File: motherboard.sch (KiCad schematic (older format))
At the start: 1 part

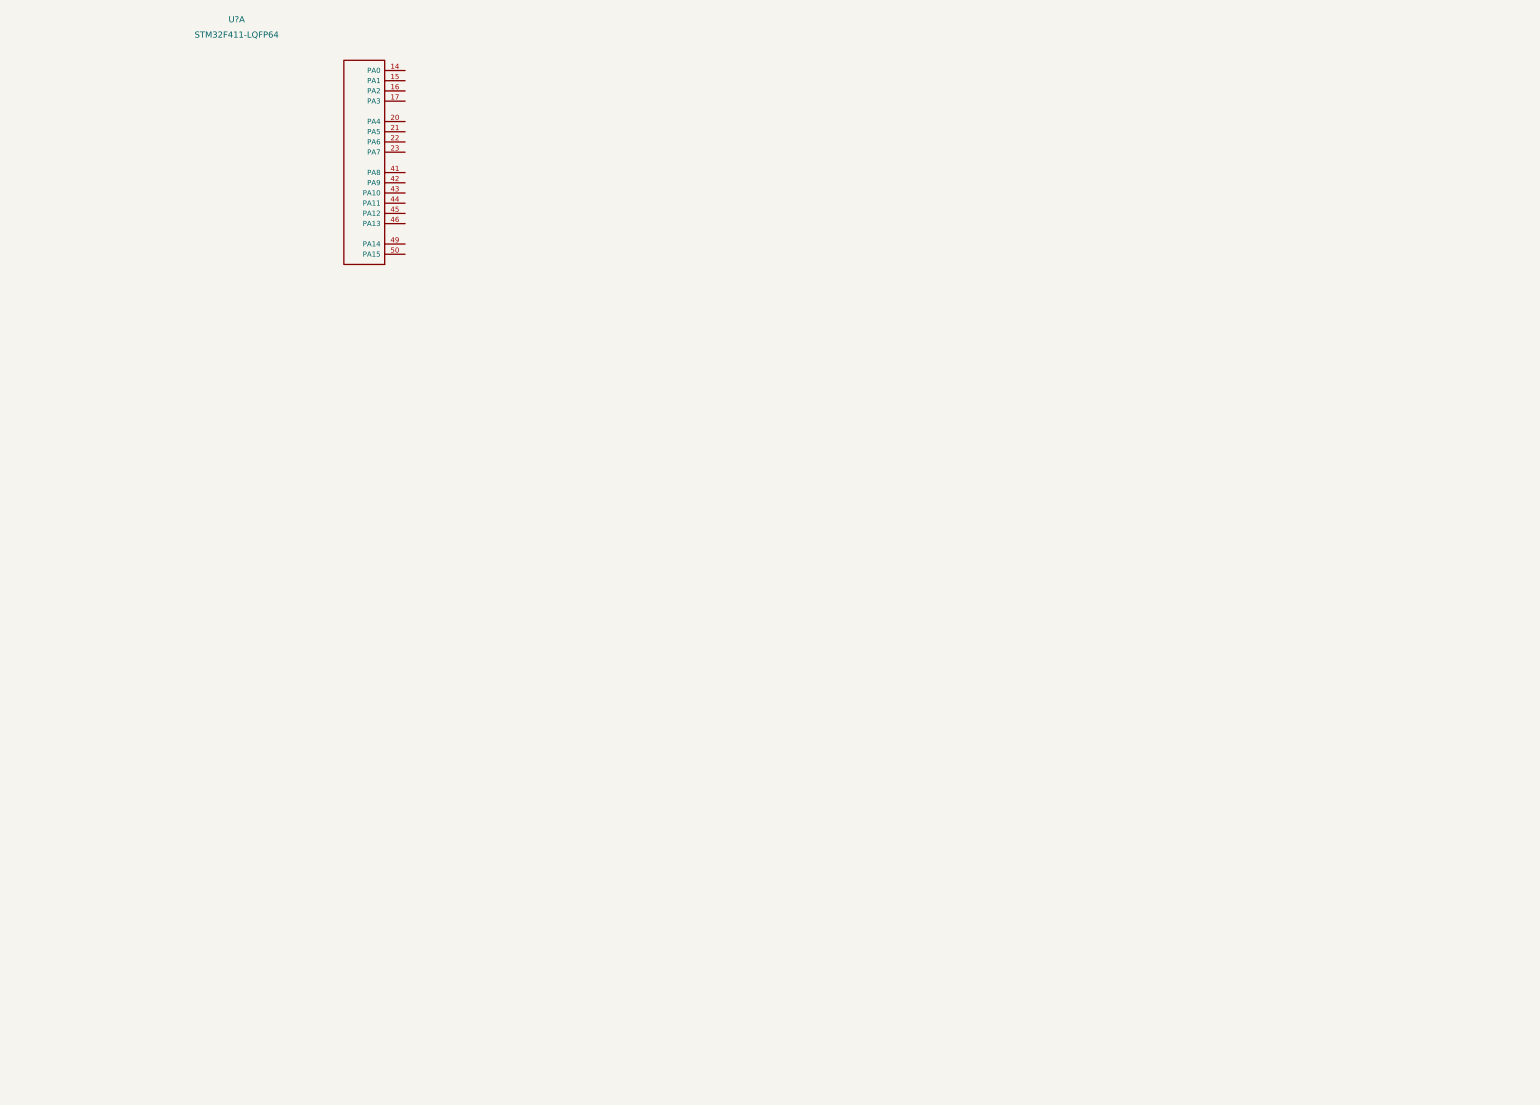
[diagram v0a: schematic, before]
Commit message: Work done on buffers and MCU placement
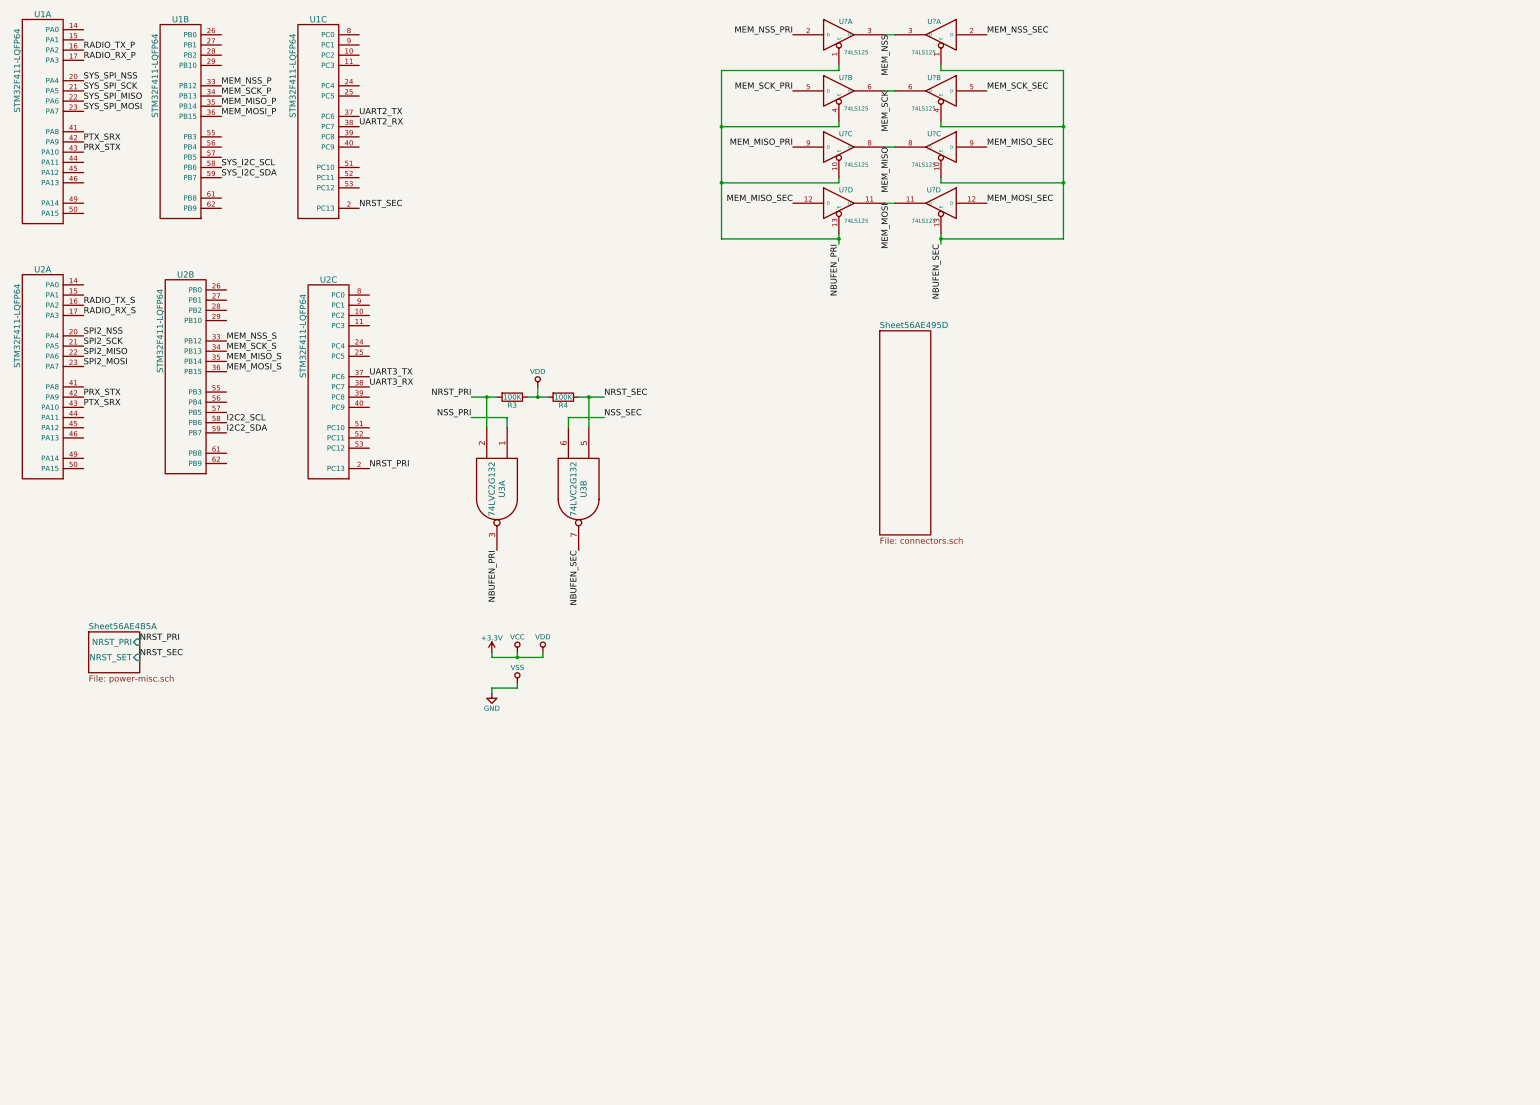
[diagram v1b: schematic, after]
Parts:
- removed U?: STM32F411-LQFP64, symbol STM32F411-LQFP64
- added R3, R4: 100K, symbol R
- added U1, U2: STM32F411-LQFP64, symbol STM32F411-LQFP64
- added U3: 74LVC2G132, symbol 74LVC2G132
- added U? (x8): 74LS125, symbol 74LS125
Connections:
- new net +3V3: R3.1, R4.2, U3.8 (VCC), U3.8 (VCC), U?.14 (VCC), U?.14 (VCC), U?.14 (VCC), U?.14 (VCC), U?.14 (VCC), U?.14 (VCC), U?.14 (VCC), U?.14 (VCC)
- new net GND: U3.4 (GND), U3.4 (GND), U?.7 (GND), U?.7 (GND), U?.7 (GND), U?.7 (GND), U?.7 (GND), U?.7 (GND), U?.7 (GND), U?.7 (GND)
- new net I2C2_SCL: U2.58 (PB6)
- new net I2C2_SDA: U2.59 (PB7)
- new net MEM_MISO: U?.8 (O), U?.8 (O)
- new net MEM_MISO_P: U1.35 (PB14)
- new net MEM_MISO_PRI: U?.9 (D)
- new net MEM_MISO_S: U2.35 (PB14)
- new net MEM_MISO_SEC: U?.12 (D), U?.9 (D)
- new net MEM_MOSI: U?.11 (O), U?.11 (O)
- new net MEM_MOSI_P: U1.36 (PB15)
- new net MEM_MOSI_S: U2.36 (PB15)
- new net MEM_MOSI_SEC: U?.12 (D)
- new net MEM_NSS: U?.3 (O), U?.3 (O)
- new net MEM_NSS_P: U1.33 (PB12)
- new net MEM_NSS_PRI: U?.2 (D)
- new net MEM_NSS_S: U2.33 (PB12)
- new net MEM_NSS_SEC: U?.2 (D)
- new net MEM_SCK: U?.6 (O), U?.6 (O)
- new net MEM_SCK_P: U1.34 (PB13)
- new net MEM_SCK_PRI: U?.5 (D)
- new net MEM_SCK_S: U2.34 (PB13)
- new net MEM_SCK_SEC: U?.5 (D)
- new net NBUFEN_PRI: U3.3, U?.1 (E), U?.10 (E), U?.13 (E), U?.4 (E)
- new net NBUFEN_SEC: U3.7, U?.1 (E), U?.10 (E), U?.13 (E), U?.4 (E)
- new net NRST_PRI: R3.2, U2.2 (PC13), U3.2
- new net NRST_SEC: R4.1, U1.2 (PC13), U3.5
- new net NSS_PRI: U3.1
- new net NSS_SEC: U3.6
- new net PRX_STX: U1.43 (PA10), U2.42 (PA9)
- new net PTX_SRX: U1.42 (PA9), U2.43 (PA10)
- new net RADIO_RX_P: U1.17 (PA3)
- new net RADIO_RX_S: U2.17 (PA3)
- new net RADIO_TX_P: U1.16 (PA2)
- new net RADIO_TX_S: U2.16 (PA2)
- new net SPI2_MISO: U2.22 (PA6)
- new net SPI2_MOSI: U2.23 (PA7)
- new net SPI2_NSS: U2.20 (PA4)
- new net SPI2_SCK: U2.21 (PA5)
- new net SYS_I2C_SCL: U1.58 (PB6)
- new net SYS_I2C_SDA: U1.59 (PB7)
- new net SYS_SPI_MISO: U1.22 (PA6)
- new net SYS_SPI_MOSI: U1.23 (PA7)
- new net SYS_SPI_NSS: U1.20 (PA4)
- new net SYS_SPI_SCK: U1.21 (PA5)
- new net UART2_RX: U1.38 (PC7)
- new net UART2_TX: U1.37 (PC6)
- new net UART3_RX: U2.38 (PC7)
- new net UART3_TX: U2.37 (PC6)

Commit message: Did some stuff
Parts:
- added R? (x2): 100K, symbol R
- added U? (x4): 74LS125, symbol 74LS125
- gave numbers to parts that had none: 2
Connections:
- net +3V3: now also U4.13 (E), U5.13 (E), R?.2, R?.2, U?.14 (VCC), U?.14 (VCC), U?.14 (VCC), U?.14 (VCC)
- net GND: now also U?.7 (GND), U?.7 (GND), U?.7 (GND), U?.7 (GND)
- net MEM_MISO: now also U4.12 (D), U5.12 (D); no longer U4.8 (O), U5.8 (O)
- net MEM_MISO_SEC: now also U4.11 (O); no longer U4.12 (D), U5.9 (D)
- net MEM_MOSI: now also U4.8 (O), U5.8 (O); no longer U4.11 (O), U5.11 (O)
- net MEM_MOSI_SEC: now also U5.11 (O), U5.9 (D); no longer U5.12 (D)
- net NBUFEN_PRI: now also R?.1, U?.1 (E), U?.10 (E); no longer U4.13 (E)
- net NBUFEN_SEC: now also R?.1, U?.13 (E), U?.4 (E); no longer U5.13 (E)
- net RADIO_TX_P: now also U?.2 (D)
- net RADIO_TX_S: now also U?.5 (D)
- net I2C2_SCL renamed SYS_SCL_S
- net SYS_SCL_S: now also U?.12 (D)
- net I2C2_SDA renamed SYS_SDA_S
- net MEM_MISO_PRI renamed MEM_MOSI_PRI
- net SYS_I2C_SCL renamed SYS_SCL_P
- net SYS_SCL_P: now also U?.9 (D)
- net SYS_I2C_SDA renamed SYS_SDA_P
- new net RADIO_TX: U?.3 (O), U?.6 (O)
- new net SYS_SCL: U?.11 (O), U?.8 (O)
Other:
- moved on the sheet: R3, R4, U2B, U2C, U3A, U3B, U4D, U5D

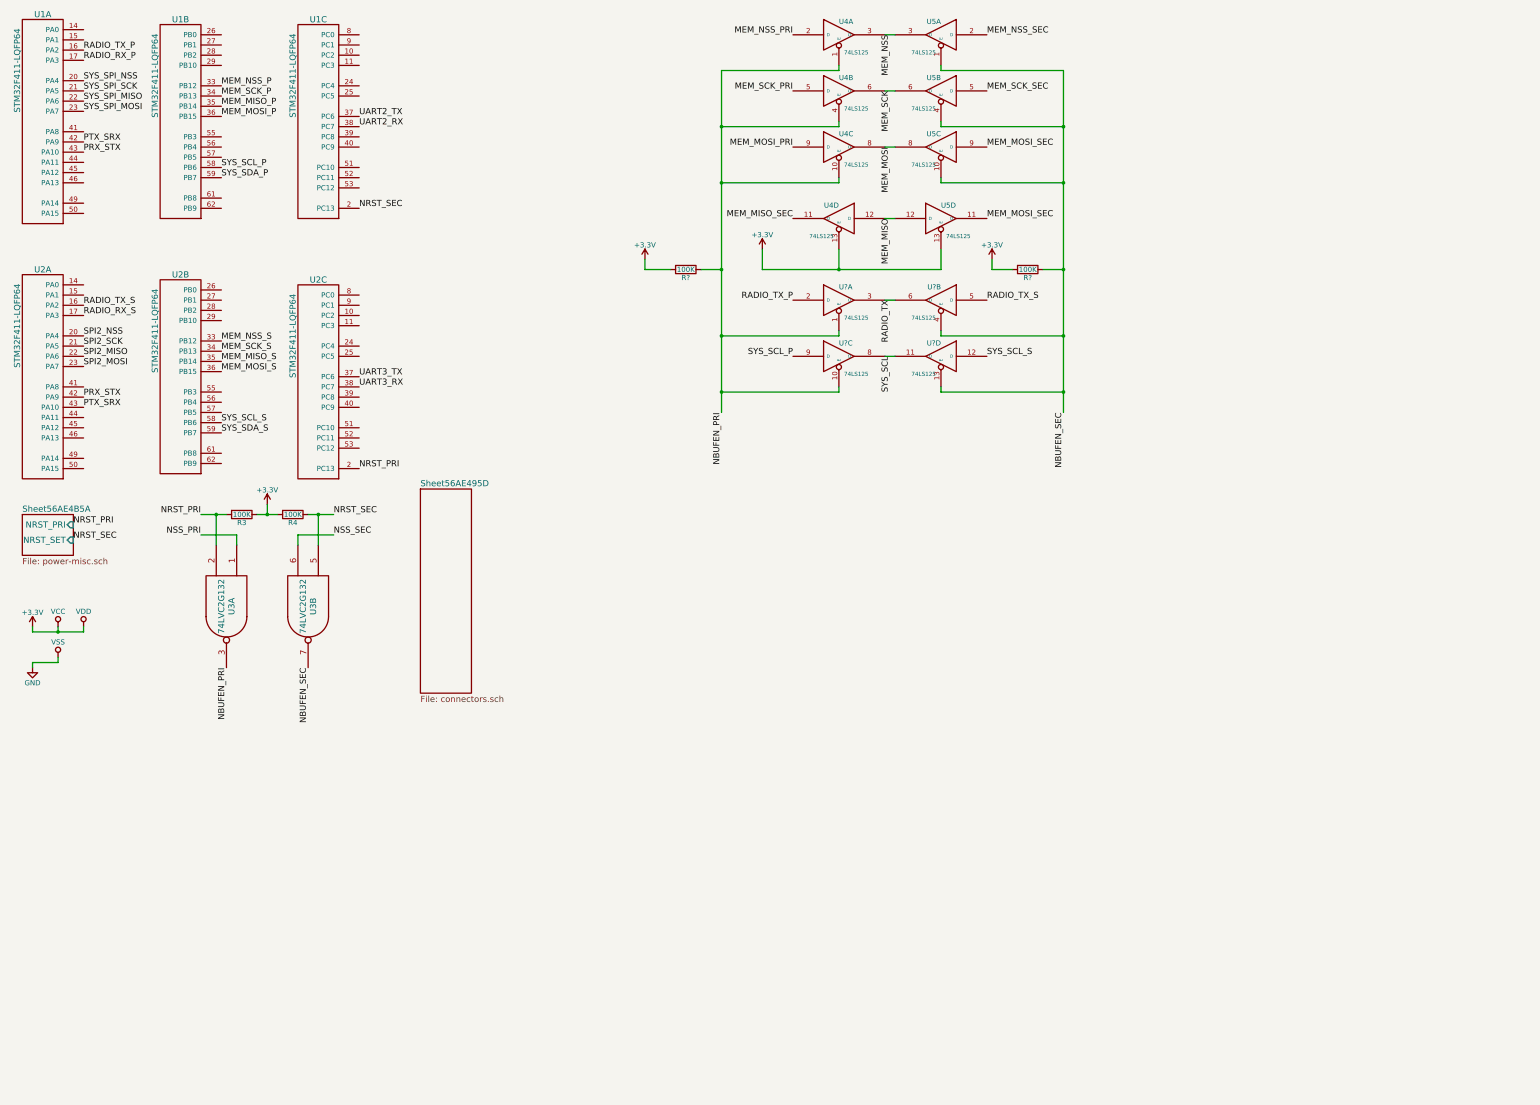
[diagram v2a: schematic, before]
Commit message: Began adding memory
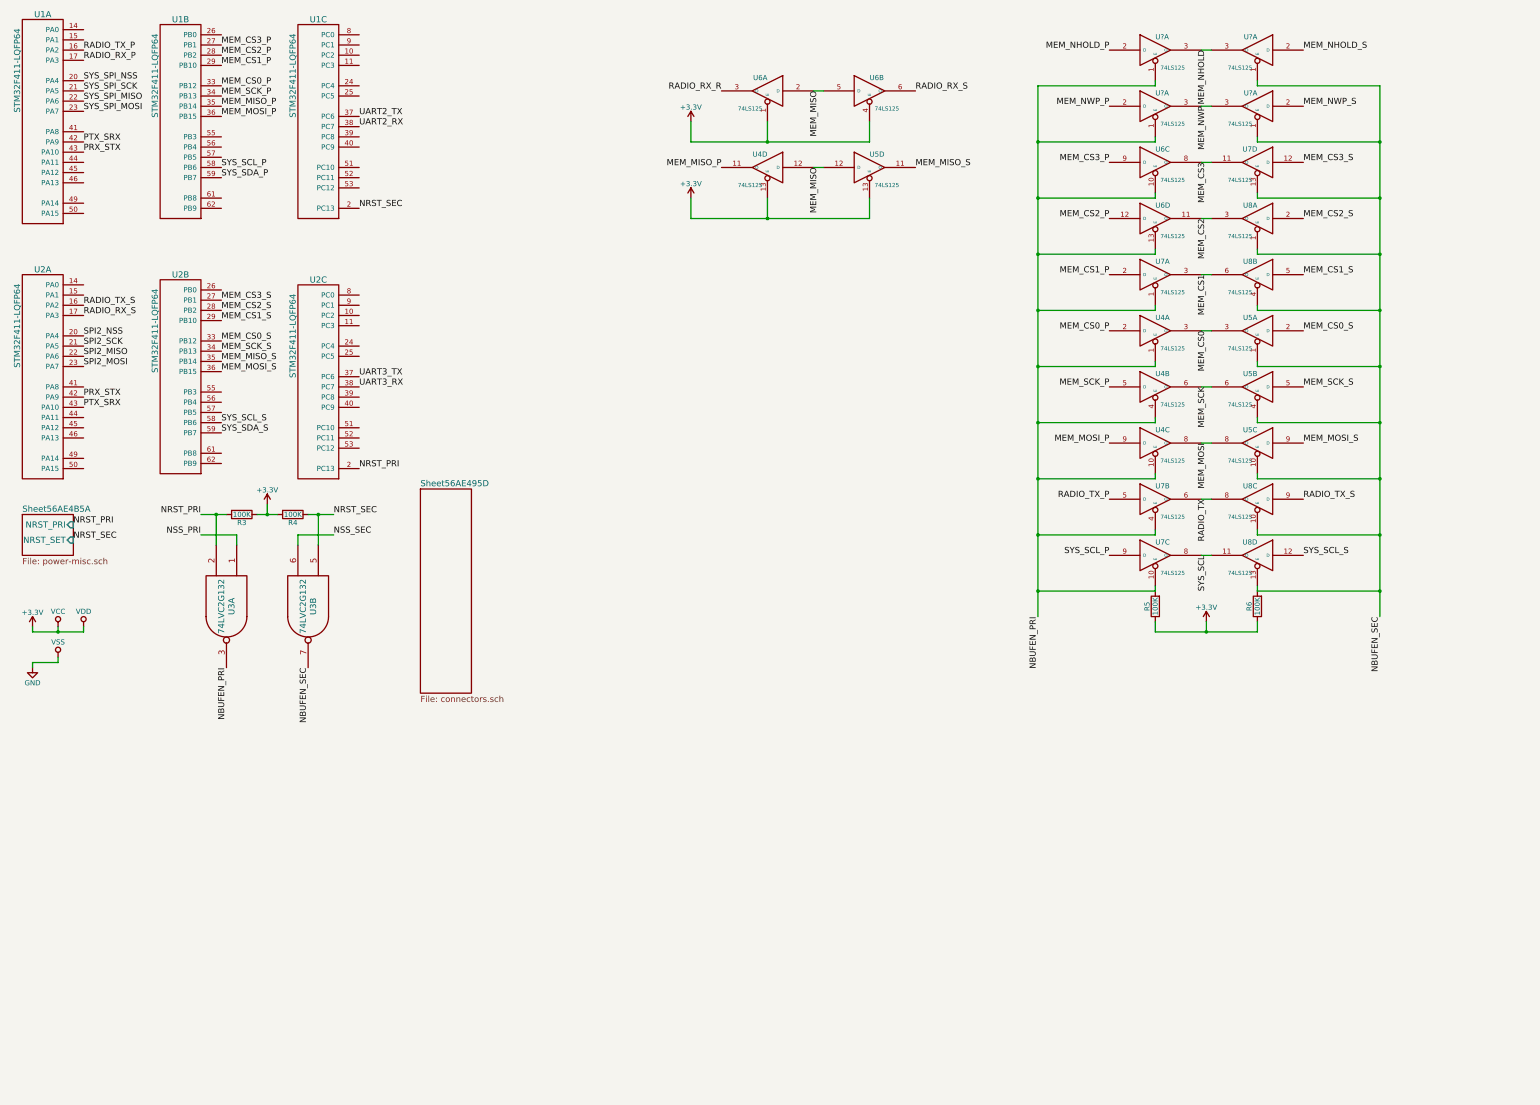
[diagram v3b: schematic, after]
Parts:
- added U6, U? (x4): 74LS125, symbol 74LS125
- added unit 4 of U7
- added unit 1 of U7
- added unit 1 of U8
- added unit 2 of U8
- gave numbers to parts that had none: 4
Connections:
- net MEM_MISO_SEC is gone; now on net MEM_MISO_P: U4.11 (O)
- net MEM_MOSI_PRI is gone; now on net MEM_MOSI_P: U4.9 (D)
- net MEM_NSS_PRI is gone; now on net MEM_CS0_P: U4.2 (D)
- net MEM_NSS_SEC is gone; now on net MEM_CS0_S: U5.2 (D)
- net MEM_SCK_PRI is gone; now on net MEM_SCK_P: U4.5 (D)
- net MEM_SCK_SEC is gone; now on net MEM_SCK_S: U5.5 (D)
- net +3V3: now also R5.1, R6.1, U6.1 (E), U6.14 (VCC), U6.14 (VCC), U6.14 (VCC), U6.14 (VCC), U6.4 (E), U7.14 (VCC), U7.14 (VCC), U8.14 (VCC), U8.14 (VCC), U?.14 (VCC), U?.14 (VCC), U?.14 (VCC), U?.14 (VCC); no longer R5.2, R6.2
- net GND: now also U6.7 (GND), U6.7 (GND), U6.7 (GND), U6.7 (GND), U7.7 (GND), U7.7 (GND), U8.7 (GND), U8.7 (GND), U?.7 (GND), U?.7 (GND), U?.7 (GND), U?.7 (GND)
- net MEM_MISO: now also U6.2 (D), U6.5 (D)
- net MEM_MISO_S: now also U5.11 (O)
- net MEM_MOSI_S: now also U5.9 (D)
- net NBUFEN_PRI: now also R5.2, U7.4 (E), U6.10 (E), U6.13 (E), U7.1 (E), U?.1 (E), U?.1 (E); no longer R5.1, U7.1 (E)
- net NBUFEN_SEC: now also R6.2, U8.10 (E), U7.13 (E), U8.1 (E), U8.4 (E), U?.1 (E), U?.1 (E); no longer R6.1, U8.4 (E)
- net RADIO_RX_S: now also U6.6 (O)
- net RADIO_TX: now also U7.6 (O), U8.8 (O); no longer U7.3 (O), U8.6 (O)
- net RADIO_TX_P: now also U7.5 (D); no longer U7.2 (D)
- net RADIO_TX_S: now also U8.9 (D); no longer U8.5 (D)
- net MEM_CS3_P: now reaches U1.27 (PB1)
- net MEM_CS3_P: now also U6.9 (D)
- net MEM_CS2_P: now reaches U1.28 (PB2)
- net MEM_CS2_P: now also U6.12 (D)
- net MEM_CS1_P: now reaches U1.29 (PB10)
- net MEM_CS1_P: now also U7.2 (D)
- net MEM_CS3_S: now reaches U2.27 (PB1)
- net MEM_CS3_S: now also U7.12 (D)
- net MEM_CS2_S: now reaches U2.28 (PB2)
- net MEM_CS2_S: now also U8.2 (D)
- net MEM_CS1_S: now reaches U2.29 (PB10)
- net MEM_CS1_S: now also U8.5 (D)
- removed net MEM_MOSI_SEC: U5.11 (O), U5.9 (D)
- net MEM_NSS renamed MEM_CS0
- net MEM_NSS_P renamed MEM_CS0_P
- net MEM_NSS_S renamed MEM_CS0_S
- new net MEM_CS1: U7.3 (O), U8.6 (O)
- new net MEM_CS2: U6.11 (O), U8.3 (O)
- new net MEM_CS3: U6.8 (O), U7.11 (O)
- new net MEM_NHOLD: U?.3 (O), U?.3 (O)
- new net MEM_NHOLD_P: U?.2 (D)
- new net MEM_NHOLD_S: U?.2 (D)
- new net MEM_NWP: U?.3 (O), U?.3 (O)
- new net MEM_NWP_P: U?.2 (D)
- new net MEM_NWP_S: U?.2 (D)
- new net RADIO_RX_R: U6.3 (O)
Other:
- moved on the sheet: R5, R6, U4A, U4B, U4C, U4D, U5A, U5B, U5C, U5D, U7C, U8D
